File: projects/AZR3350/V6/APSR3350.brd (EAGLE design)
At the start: 80.5 x 100 mm, 212 parts, among them IC1 A4403, IC10 A4988, IC2 LDO-TS1117CW-3V3, IC3 ATSAM4S8C, IC4 74AHC08, IC7 A4988, IC8 A4988, IC9 A4988, J1 ZX62-AB-5PA, J2 MOLEX-SD-47571-001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

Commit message: Progress on APSR
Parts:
- added F2, F3: (no value), fuse:19560
- moved C15 206.0 mm to (86.5, -2.00)
- moved C16 206.0 mm to (98.5, -12.0)
- moved C17 206.0 mm to (91.5, -12.0)
- moved C18 206.0 mm to (152.5, 3.00)
- moved C19 206.0 mm to (147.5, 3.00)
- moved C20 206.0 mm to (85.5, -12.0)
- moved C21 206.0 mm to (79.5, -12.0)
- moved C22 206.0 mm to (72.5, -12.0)
- moved C23 206.0 mm to (66.5, -12.0)
- moved C24 206.0 mm to (161.5, -7.00)
- moved C25 206.0 mm to (66.5, -30.0)
- moved C26 206.0 mm to (155.5, -7.00)
- moved C27 206.0 mm to (89.5, -24.0)
- moved C28 206.0 mm to (142.5, 3.00)
- moved C9 206.0 mm to (164.5, -24.0)
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- renumbered USB to USB_L
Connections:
- removed net +12V: D1.A, PWRIN.1, R1.2
- new net BED_FUSED: F3.2, J3.2, R43.2
- new net EXT_FUSED: F2.2, J3.4, R42.2
- net +24V: now also D1.A, F2.1, F3.1, PWRIN.1, R1.2; no longer J3.2, J3.4, R42.2, R43.2
- net BED_D: now also J3.1; no longer J3.3
- net EXT_D: now also J3.3; no longer J3.1
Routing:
- net GND: track 0.00 -> 700.6 mm, vias 0 -> 91
- net +3V3: track 0.00 -> 212.6 mm, vias 0 -> 20
- net +24V: track 0.00 -> 124.3 mm, vias 0 -> 20
- net DET: track 0.00 -> 18.4 mm
- net VIN: track 0.00 -> 14.6 mm
- net VOUT: track 0.00 -> 13.5 mm
- net VIN_F: track 0.00 -> 13.0 mm
- net BED_FUSED: track 0.00 -> 12.7 mm
- net EXT_FUSED: track 0.00 -> 12.6 mm
- net DAT2: track 0.00 -> 12.4 mm
- net RSTZ: track 0.00 -> 12.2 mm
- net RSTY: track 0.00 -> 12.2 mm
- net RSTX: track 0.00 -> 12.2 mm
- net RSTE: track 0.00 -> 12.2 mm
- net ZMOT2B: track 0.00 -> 11.6 mm
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- added copper zone on layer 1, net +24V
- added copper zone on layer 16, net +24V
- added copper zone on layer 1, net +3V3
- added copper zone on layer 16, net +3V3
- added copper zone on layer 1, net +5V
- added copper zone on layer 1, net BED_D
- added copper zone on layer 16, net BED_D
- added copper zone on layer 1, net EMOT1A
- added copper zone on layer 1, net EMOT1B
- added copper zone on layer 1, net EMOT2A
- added copper zone on layer 1, net EMOT2B
- added copper zone on layer 1, net EXT_D
- added copper zone on layer 16, net EXT_D
- added copper zone on layer 1, net GND
- added copper zone on layer 16, net GND
- added copper zone on layer 1, net LX
- added copper zone on layer 1, net VOUT
- added copper zone on layer 1, net XMOT1A
- added copper zone on layer 1, net XMOT1B
- added copper zone on layer 1, net XMOT2A
- added copper zone on layer 1, net XMOT2B
- added copper zone on layer 1, net YMOT1A
- added copper zone on layer 1, net YMOT1B
- added copper zone on layer 1, net YMOT2A
- added copper zone on layer 1, net YMOT2B
- added copper zone on layer 1, net ZMOT1A
- added copper zone on layer 1, net ZMOT1B
- added copper zone on layer 1, net ZMOT2A
- added copper zone on layer 1, net ZMOT2B
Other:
- outline, holes or cut-outs redrawn

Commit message: Progress on APSR
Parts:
- moved C18 120.6 mm to (33.5, 22.5)
- moved C19 104.9 mm to (46.5, 31.5)
- moved C16 75.0 mm to (33.0, 24.5)
- moved C27 74.0 mm to (39.5, 30.5)
- moved R13 63.1 mm to (45.5, 30.0)
- moved C29 20.8 mm to (52.2, 32.0), turned to 0 degrees
- moved C14 14.7 mm to (48.8, 28.6), turned to 270 degrees
- moved X1 14.1 mm to (52.2, 28.3), turned to 90 degrees
- moved C13 12.6 mm to (52.3, 24.6)
- moved C30 12.3 mm to (55.0, 27.2), turned to 90 degrees
- moved C11 5.22 mm to (41.5, 5.50)
- moved C10 5.00 mm to (33.5, 15.5), turned to 270 degrees
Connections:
- net N$1 renamed IDEK
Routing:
- net USB_P: track 5.60 -> 35.5 mm
- net USB_N: track 5.59 -> 35.5 mm
- net GND: track 700.6 -> 723.6 mm, vias 91 -> 93
- net ERASE: track 0.00 -> 10.2 mm
- net +3V3: track 212.6 -> 222.0 mm
- net XIN: track 0.00 -> 8.45 mm
- net XOUT: track 0.00 -> 7.20 mm

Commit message: Progress, as usual
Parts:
- removed JP1: (no value), pinhead:1X05
- removed Y_STOP1: KK-254-3, con-other:MOLEX-KK-254-3
- added E_STOP: KK-254-3, con-other:MOLEX-KK-254-3
- added JP3: (no value), pinhead:1X04
- ERASE: device jumper:JP1 -> SparkFun-Connectors:1X02
- moved JP2 205.0 mm to (49.0, 68.5), turned to 90 degrees
- moved IC4 186.8 mm to (54.0, 64.5), turned to 180 degrees
- moved R42 173.3 mm to (-3.50, 93.5)
- moved R43 173.3 mm to (-3.50, 88.5)
- moved R21 172.9 mm to (28.2, 4.30), turned to 180 degrees
- moved R20 167.8 mm to (25.6, 2.40), turned to 270 degrees
- moved Q4 163.1 mm to (57.4, 23.5), turned to 225 degrees
- moved R19 157.2 mm to (25.5, 13.5)
- moved R18 154.4 mm to (25.5, 11.4)
- moved R17 151.7 mm to (25.5, 9.30)
- moved R15 149.6 mm to (25.5, 6.50)
- moved R44 148.6 mm to (57.2, 27.5), turned to 270 degrees
- moved SG1 142.4 mm to (69.3, 25.6), turned to 90 degrees
- moved C35 138.6 mm to (10.2, 19.1), turned to 180 degrees
- moved Z_STOP 134.5 mm to (43.0, 64.0), turned to 180 degrees
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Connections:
- net N$2 renamed CON
- net N$4 renamed V_FAN
- net N$7 renamed BEEP_G
- net N$8 renamed BEEP_OUT
- removed net LCD_KILL: IC3.84, JP1.4
- removed net LCD_MISO: IC3.53
- removed net LCD_SD_CS: IC3.80
- net +3V3: now also E_STOP.2; no longer Y_STOP1.2
- net BED: now also IC3.24; no longer IC3.30
- net BEEPER: now also IC3.92; no longer IC3.86
- net BTN_EN1: now also IC3.83, JP3.1; no longer IC3.82, JP1.1
- net BTN_EN2: now also IC3.82, JP3.2; no longer IC3.83, JP1.2
- net BTN_ENC: now also IC3.80, JP3.3; no longer IC3.71, JP1.3
- net ESP_DATA_RDY: now also IC3.32; no longer IC3.22
- net ESP_RST: now also IC3.43; no longer IC3.37
- net E_DIR: now also IC3.74; no longer IC3.43
- net E_EN: now also IC3.72; no longer IC3.48
- net E_STEP: now also IC3.73; no longer IC3.47
- net E_STOP_IN: now also E_STOP.1; no longer Y_STOP1.1
- net GND: now also E_STOP.3, JP3.4; no longer JP1.5, Y_STOP1.3
- net HOTEND: now also IC3.25; no longer IC3.40
- net RESET: now also RESET.A'
- net SAM_TFR_RDY: now also IC3.40; no longer IC3.21
- net T_BED: now also IC3.20; no longer IC3.19
- net T_EXT: now also IC3.21; no longer IC3.20
- net URXD1: now also IC3.44; no longer IC3.7
- net UTXD1: now also IC3.46; no longer IC3.9
- net X_DIR: now also IC3.28; no longer IC3.72
- net X_EN: now also IC3.30; no longer IC3.74
- net X_STEP: now also IC3.29; no longer IC3.73
- net Y_DIR: now also IC3.35; no longer IC3.62
- net Y_EN: now also IC3.38; no longer IC3.66
- net Y_STEP: now also IC3.37; no longer IC3.65
- net Z_DIR: now also IC3.55; no longer IC3.51
- net Z_EN: now also IC3.49; no longer IC3.55
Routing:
- net +24V: track 124.3 -> 325.2 mm, vias 20 -> 36
- net GND: track 723.6 -> 915.9 mm, vias 93 -> 125
- net LCD_MOSI: track 0.00 -> 77.1 mm, vias 0 -> 2
- net LCD_CS: track 0.00 -> 54.3 mm, vias 0 -> 3
- net Z_DIR: track 1.89 -> 55.3 mm, vias 1 -> 2
- net Z_STEP: track 1.44 -> 51.9 mm, vias 1 -> 3
- net UTXD1: track 0.00 -> 46.1 mm, vias 0 -> 2
- net NPCS0: track 0.00 -> 45.0 mm, vias 0 -> 2
- net X_EN: track 10.5 -> 55.0 mm, vias 2 -> 3
- net X_DIR: track 1.89 -> 46.2 mm, vias 1 -> 2
- net VSSA: track 0.00 -> 43.9 mm
- net X_STEP: track 1.44 -> 44.4 mm, vias 1 -> 2
- net ADVREF: track 0.00 -> 41.2 mm
- net Y_EN: track 10.5 -> 51.2 mm, vias 2 -> 3
- net Y_STEP: track 1.44 -> 40.4 mm, vias 1 -> 2
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
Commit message: More progress
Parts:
- RESET: value (none) -> EVQP7J; device misc:EVQQ2 -> misc:EVQP7
- moved R45 130.1 mm to (51.7, 68.7), turned to 270 degrees
- moved RESET 105.5 mm to (32.4, 1.50)
- moved C38 93.1 mm to (57.7, 62.9)
- moved R14 59.4 mm to (37.1, 1.60)
- moved C28 53.5 mm to (32.5, 4.10), turned to 180 degrees
- moved C67 43.5 mm to (-17.0, 60.5)
- moved C68 43.5 mm to (-22.0, 60.5)
- moved EXT_L 29.0 mm to (12.0, 71.5)
- moved R42 26.7 mm to (10.0, 70.5), turned to 90 degrees
- moved BED_L 18.8 mm to (11.0, 82.0), turned to 90 degrees
- moved R43 16.8 mm to (11.0, 80.0), turned to 180 degrees
- moved ERASE 7.53 mm to (73.5, 17.0)
- moved Y_STOP 1.41 mm to (32.5, 63.0)
- moved C24 1.26 mm to (57.7, 19.8)
- moved X_STOP 1.00 mm to (32.5, 71.5)
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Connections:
- removed net PWR_FAIL_DET: IC3.23
- net E_STOP: now also IC3.49; no longer IC3.75
- net GND: now also RESET.2A, RESET.2B; no longer RESET.B, RESET.B'
- net LCD_CS: now also IC4.12; no longer IC4.13
- net LCD_SCK: now also IC4.13; no longer IC4.12
- net PWR_FAIL_DET2: now also IC3.23
- net RESET: now also RESET.1A, RESET.1B; no longer RESET.A, RESET.A'
- net X_STOP: now also IC3.19; no longer IC3.79
- net Y_STOP: now also IC3.22; no longer IC3.78
- net Z_EN: now also IC3.51; no longer IC3.49
- net Z_STOP: now also IC3.62; no longer IC3.76
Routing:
- net +3V3: track 232.1 -> 364.1 mm, vias 20 -> 31
- net GND: track 915.9 -> 1017.3 mm, vias 125 -> 137
- net Z_STOP: track 0.00 -> 76.2 mm, vias 0 -> 1
- net LCD_SCK: track 0.00 -> 60.4 mm, vias 0 -> 2
- net E_STOP: track 0.00 -> 59.1 mm, vias 0 -> 1
- net +5V: track 27.4 -> 83.2 mm, vias 0 -> 1
- net BED: track 0.00 -> 49.8 mm, vias 0 -> 1
- net PWR_FAIL_DET2: track 0.00 -> 49.4 mm, vias 0 -> 1
- net VDDOUT: track 29.1 -> 75.7 mm
- net +24V: track 325.2 -> 282.3 mm, vias 36 -> 28
- net Y_STOP: track 6.16 -> 48.9 mm, vias 0 -> 1
- net E_DIR: track 1.89 -> 44.5 mm, vias 1 -> 2
- net X_STOP: track 6.43 -> 48.3 mm, vias 0 -> 1
- net E_STEP: track 1.44 -> 41.2 mm, vias 1 -> 2
- net RESET: track 0.00 -> 35.8 mm, vias 0 -> 2
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
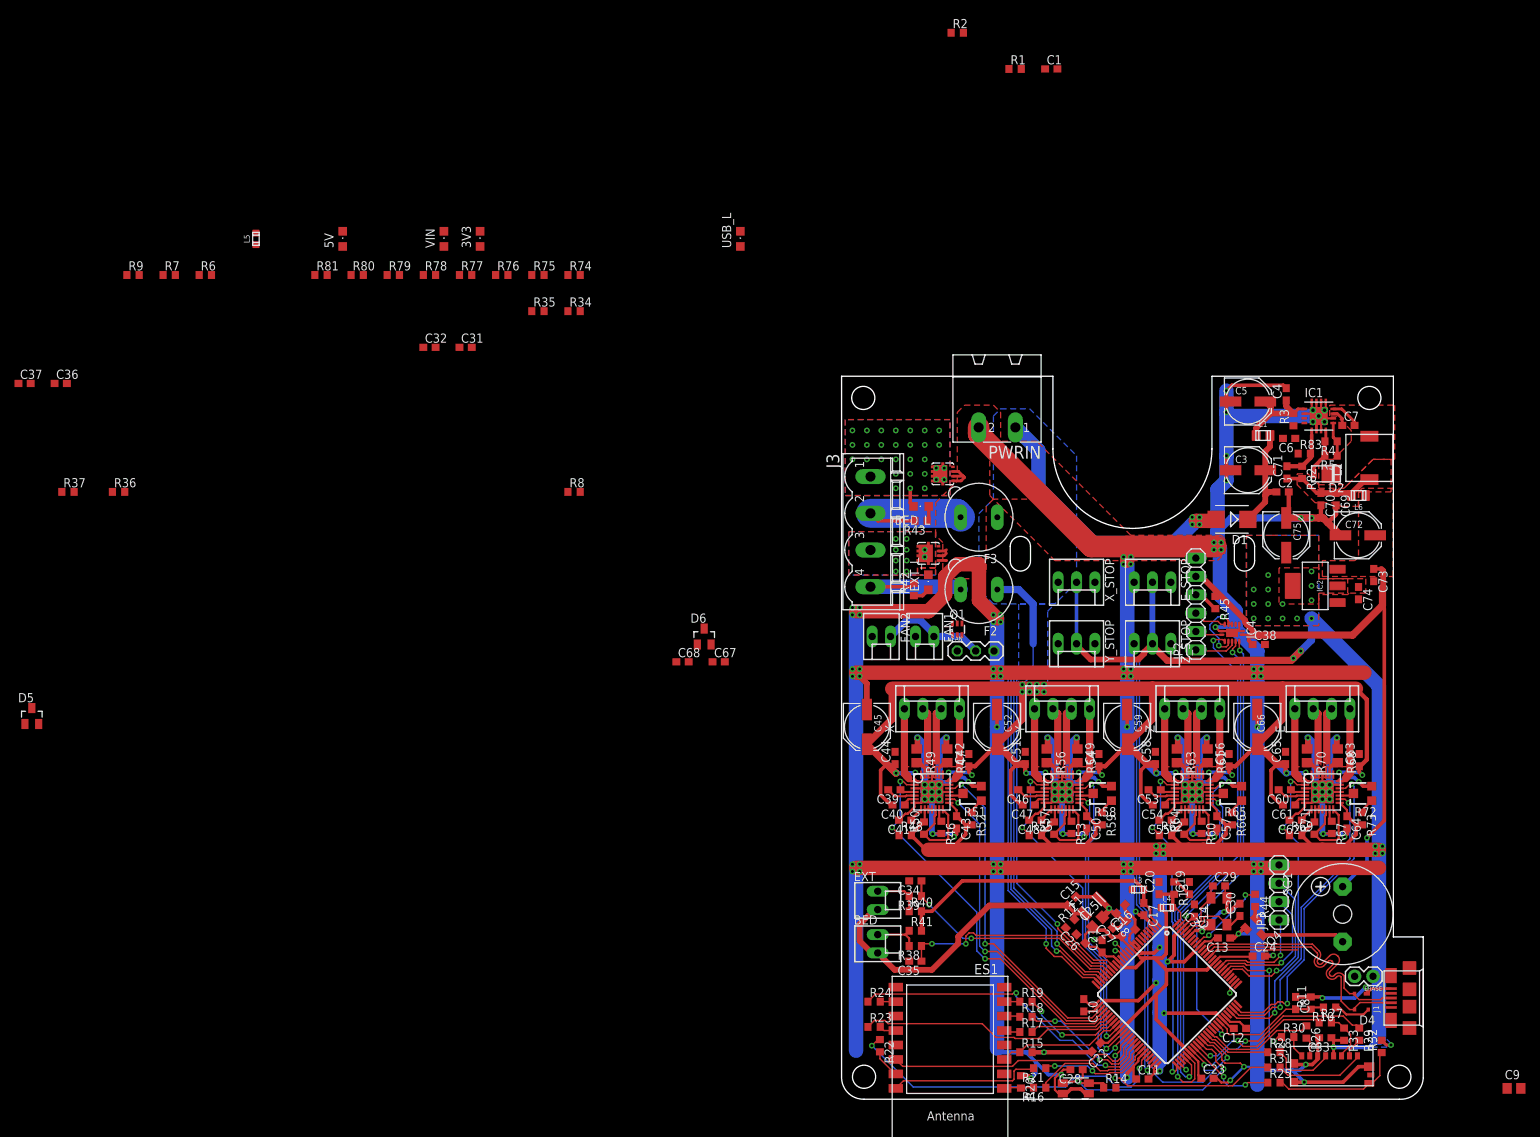
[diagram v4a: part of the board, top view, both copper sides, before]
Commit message: All placed and routed
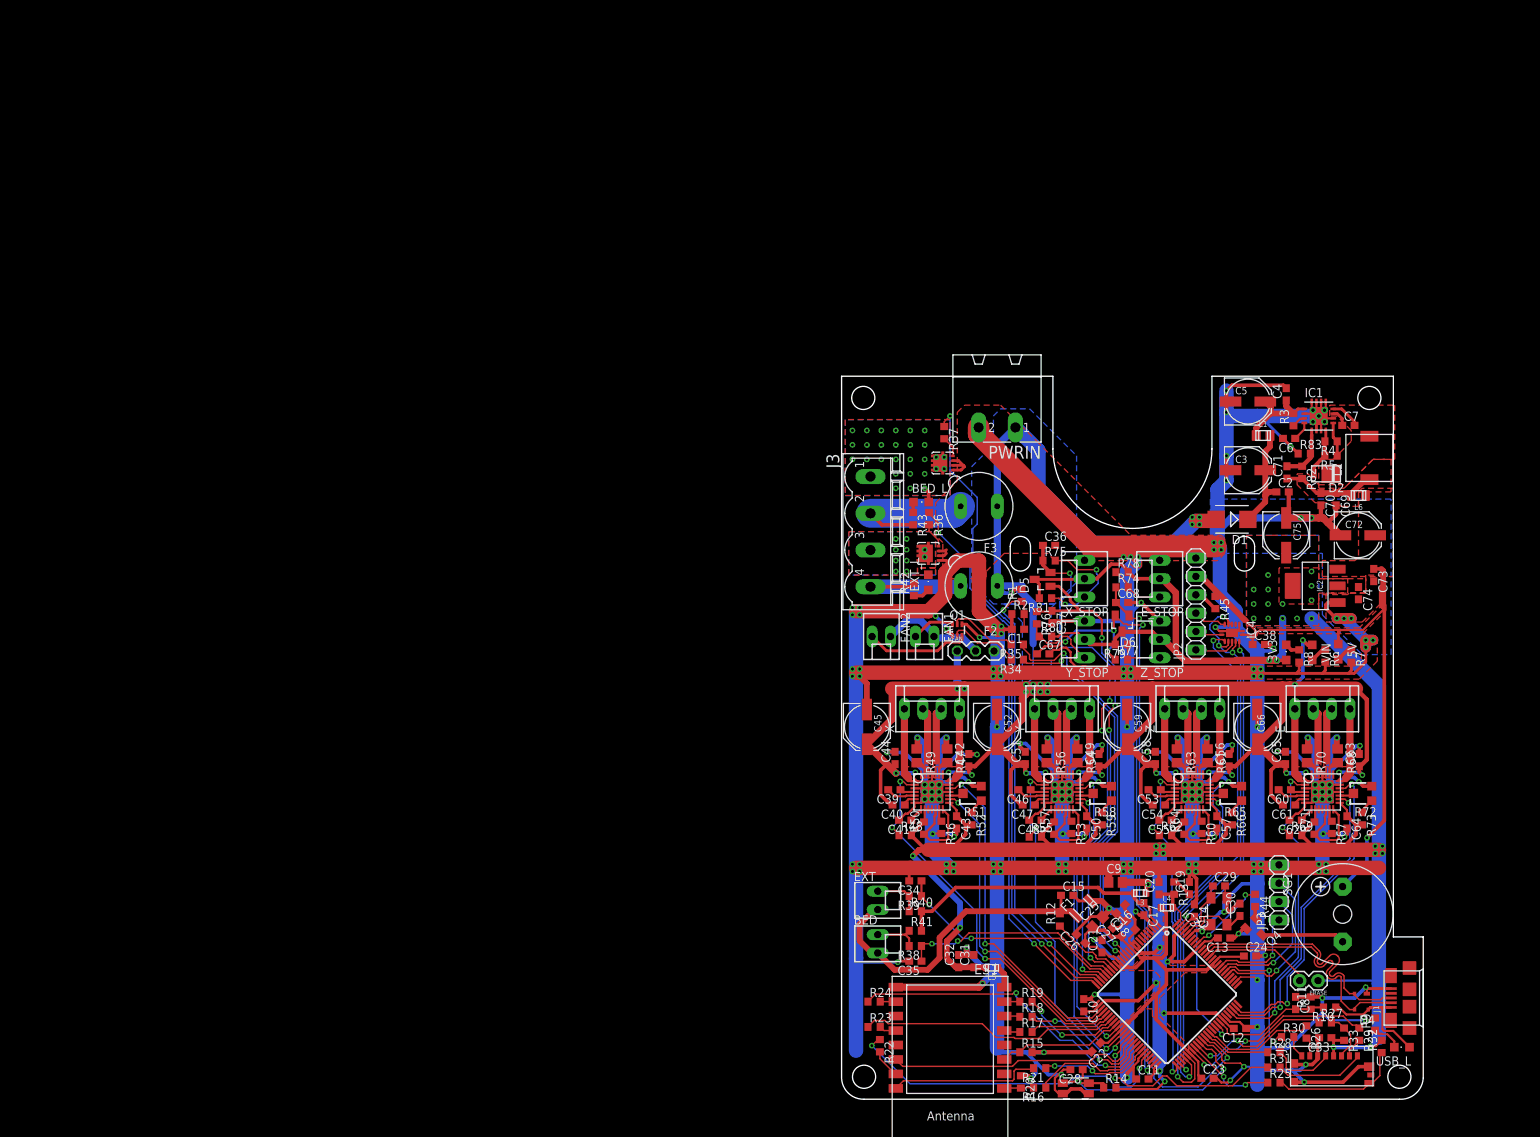
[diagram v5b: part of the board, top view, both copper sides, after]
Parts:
- moved R9 200.6 mm to (73.8, 10.4), turned to 90 degrees
- moved R7 171.8 mm to (70.5, 61.3), turned to 270 degrees
- moved R6 163.6 mm to (66.9, 61.3), turned to 270 degrees
- moved 5V 149.1 mm to (68.7, 61.9), turned to 180 degrees
- moved C37 145.7 mm to (29.1, 66.7), turned to 270 degrees
- moved USB_L 144.5 mm to (77.5, 7.20), turned to 90 degrees
- moved L5 143.3 mm to (20.8, 18.2), turned to 90 degrees
- moved D5 141.1 mm to (27.8, 71.9), turned to 90 degrees
- moved C36 138.5 mm to (28.7, 76.6)
- moved VIN 133.0 mm to (65.1, 61.8), turned to 180 degrees
- moved 3V3 125.3 mm to (61.5, 61.8)
- moved R37 121.5 mm to (14.2, 92.2), turned to 270 degrees
- moved R79 112.9 mm to (38.7, 62.9), turned to 180 degrees
- moved R36 112.2 mm to (12.1, 80.3), turned to 270 degrees
- moved C32 112.1 mm to (16.2, 19.1), turned to 90 degrees
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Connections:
- net X_STOP: now also C37.1, D5.1, R76.1; no longer C36.1, D5.2, R75.1
- net X_STOP_IN: now also R76.2, R80.1, Y_STOP.1; no longer R75.2, R81.1, X_STOP.1
- net Y_STOP: now also C36.1, D5.2, R75.1; no longer C37.1, D5.1, R76.1
- net Y_STOP_IN: now also R75.2, R81.1, X_STOP.1; no longer R76.2, R80.1, Y_STOP.1
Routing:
- net GND: track 1017.3 -> 1330.2 mm, vias 137 -> 179
- net HOTEND: track 0.00 -> 76.7 mm, vias 0 -> 2
- net +3V3: track 364.1 -> 436.8 mm, vias 31 -> 35
- net FAN2: track 2.20 -> 54.4 mm, vias 1 -> 2
- net FAN1: track 1.58 -> 52.0 mm, vias 1 -> 2
- net BED: track 49.8 -> 90.7 mm, vias 1 -> 2
- net +24V: track 282.3 -> 321.8 mm, vias 28 -> 33
- net Z_STOP: track 76.2 -> 103.9 mm, vias 1 -> 5
- net Y_STOP: track 48.9 -> 73.2 mm, vias 1 -> 4
- net X_STOP: track 48.3 -> 68.2 mm, vias 1 -> 4
- net Y_STOP_IN: track 0.00 -> 16.2 mm, vias 0 -> 2
- net PWR_FAIL_DET2: track 49.4 -> 65.0 mm, vias 1 -> 2
- net FAN2_D: track 0.00 -> 14.4 mm
- net E_STOP: track 59.1 -> 71.0 mm, vias 1 -> 2
- net VBUS: track 5.18 -> 16.3 mm
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- added copper zone on layer 1, net VDDOUT

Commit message: Done**
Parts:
- moved C43 0.05 mm to (15.9, 38.4)
- moved C50 0.05 mm to (33.9, 38.4)
- moved C57 0.05 mm to (51.9, 38.4)
- moved C64 0.05 mm to (69.9, 38.4)
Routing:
- net GND: track 1330.2 -> 1303.4 mm
- net +3V3: track 436.8 -> 438.0 mm

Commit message: Minor improvements, cam
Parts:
- moved R14 1.36 mm to (36.3, 2.70), turned to 135 degrees
- moved C22 0.81 mm to (34.5, 7.60), turned to 180 degrees
- moved RESET 0.10 mm to (32.3, 1.50)
- renumbered ES1 to ESP8266, JP2 to J4, JP3 to J5, SG1 to BEEPER
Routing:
- net Y_STOP: track 73.2 -> 70.9 mm
- net +3V3: track 438.0 -> 436.6 mm, vias 35 -> 34
- net Z_STOP: track 103.7 -> 102.6 mm
- net SD_CD: track 12.9 -> 12.2 mm
- net GND: track 1303.4 -> 1302.7 mm, vias 179 -> 178
- net MCDA2: track 30.2 -> 29.6 mm
- net VDDOUT: track 74.5 -> 75.0 mm
- net BED_D: track 2.13 -> 2.63 mm
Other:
- board text added: "+"
- board text added: "+24V"
- board text added: "-"
- board text added: "1"
- board text added: "2"
- board text added: "BED"
- board text added: "Designed by Ethan Tillison"
- board text added: "E"
- board text added: "ENDSTOPS"
- board text added: "EXT"
- board text added: "FANS"
- board text added: "GND"
- board text added: "PS4SR3350"
- board text added: "RESET"
- board text added: "Rev. 1.0.6"
- board text added: "THERMISTORS"
- board text added: "USB"
- board text added: "X"
- board text added: "Y"
- board text added: "Z"
- board text added: "microSD"
